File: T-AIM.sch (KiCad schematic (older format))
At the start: 21 parts, among them IC1 ATMEGA328PB-A

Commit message: Components wired
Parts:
- added C?: 1u, symbol CP1
- added C?: 10n, symbol CP1
- added C? (x2): 0.1u, symbol C
- added R?: 4.7k, symbol R
- added R?: 1k, symbol R
- added R?: 150, symbol R
- J?: value JY-MCU HC-05 Bluetooth Pins -> JY-MCU HC-05 Pins
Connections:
- net CS is gone; now on net 5V: J?.3 (P3)
- net VOUT is gone; now on net 5V: J?.2 (P2)
- net +9V: now also R?.1, R?.1, R?.1; no longer IC?.3 (VDD)
- net 5V: now also C?.1; no longer C?.1, C?.2, IC1.4 (VCC), R?.2, U?.VO
- net GND: now also IC?.1 (CTG), IC?.9 (EP), R?.2, C?.2, C?.2, C?.2; no longer C?.1
- net at IC1.18 (AVCC): now also C?.1, IC1.4 (VCC), U?.VO
- net at IC?.2 (CELL): now also C?.1, R?.2
- net BatteryLowAlert: now reaches IC?.5 (ALRT)
- net BatteryLowAlert: now also R?.2
- net FuelGaugeRestart: now reaches IC?.6 (QSTRT)
- net EN: now reaches J?.1 (P1)
- net State: now reaches J?.6 (P6)
- new net: C?.1, IC?.3 (VDD), R?.2
- no-connect marks 19 -> 18
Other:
- note added: "Alarm buzzer"
- note added: "Battery fuel gauge"
- note added: "Bluetooth Module"
- note added: "Interface Buttons"
- note added: "Sensors"
- note added: "Status LEDs"
- note added: "Voltage regulator"
- moved on the sheet: BZ?, C?, D?, IC1, IC?, J?, R?, SW?, U?

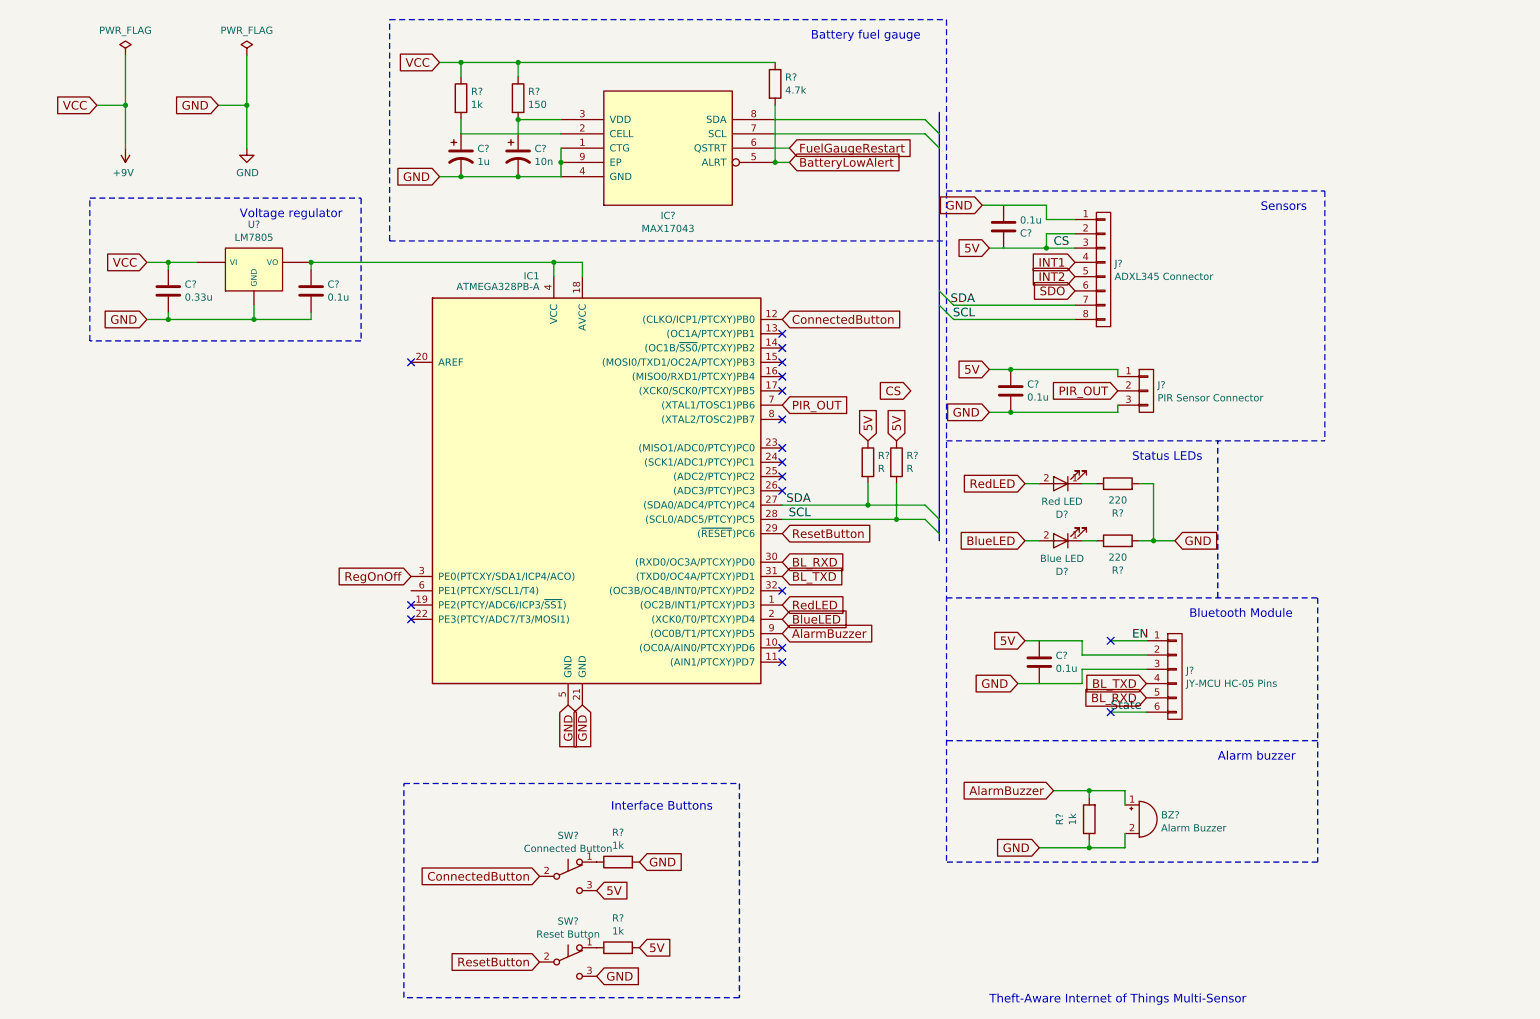
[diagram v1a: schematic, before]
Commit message: Schematics tidied up, added Vcc caps in front of MCU
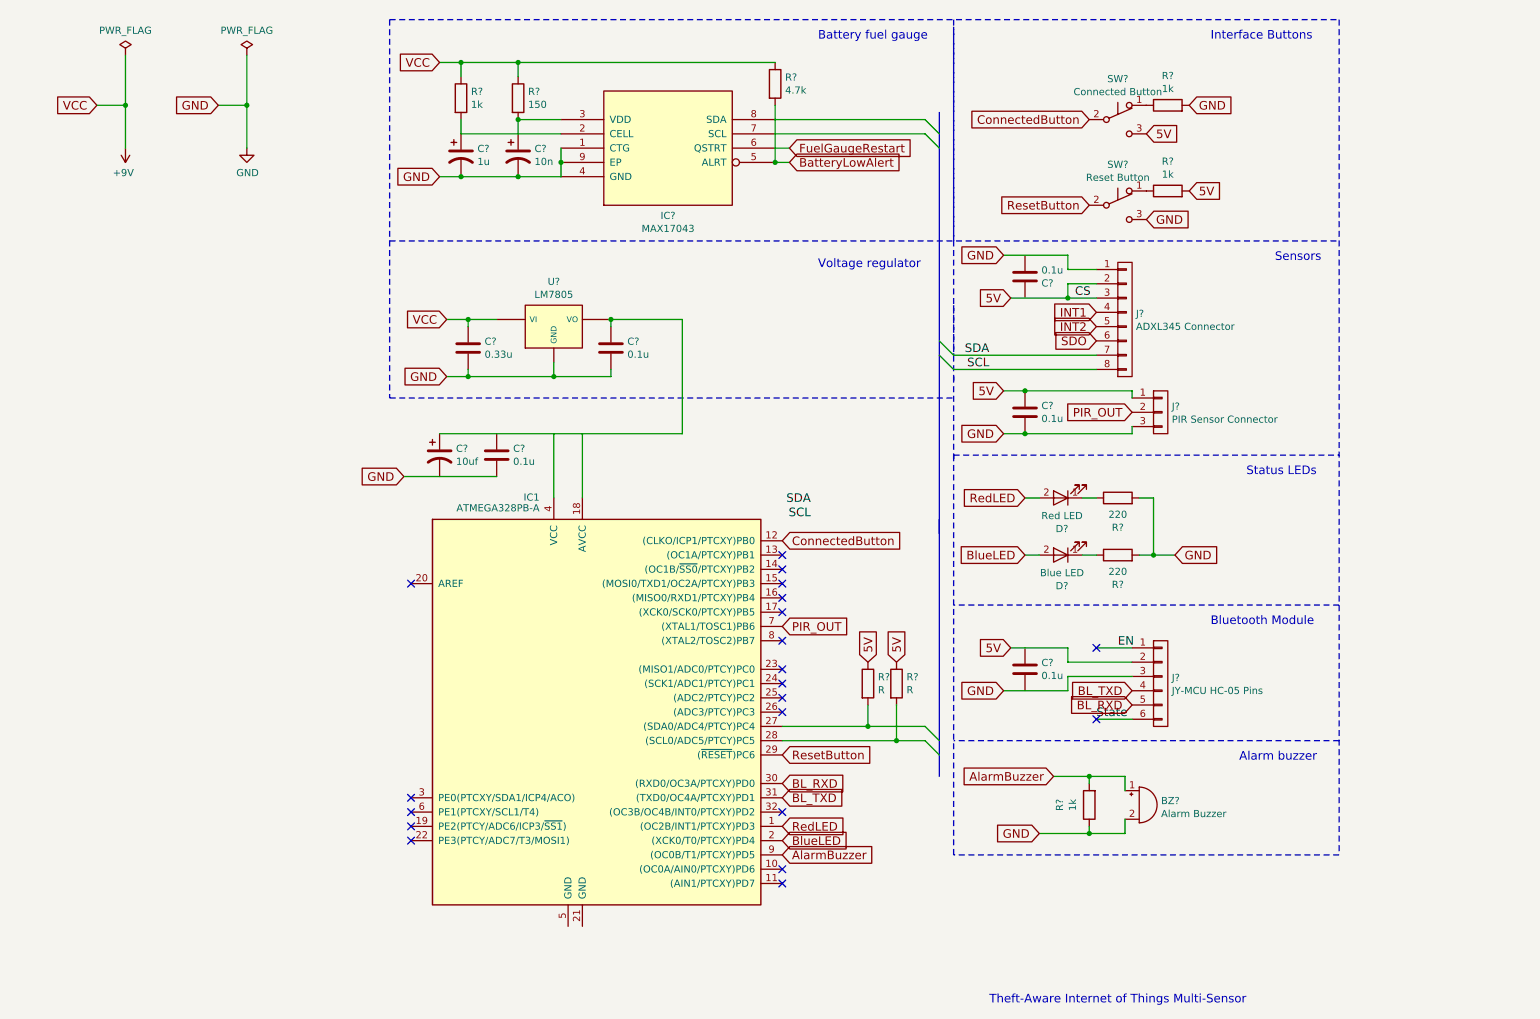
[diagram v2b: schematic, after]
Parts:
- added C?: 0.1u, symbol C
- added C?: 10uf, symbol CP1
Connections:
- net GND: now also C?.2; no longer IC1.21 (GND), IC1.5 (GND)
- net SCL: no longer IC1.28 ((SCL0/ADC5/PTCY)PC5), R?.2
- net SDA: no longer IC1.27 ((SDA0/ADC4/PTCY)PC4), R?.2
- net at C?.1, U?.VO: now also C?.1; no longer IC1.18 (AVCC), IC1.4 (VCC)
- net RegOnOff: no longer names the net of IC1.3 (PE0(PTCXY/SDA1/ICP4/ACO))
- new net: IC1.27 ((SDA0/ADC4/PTCY)PC4), R?.2
- new net: IC1.28 ((SCL0/ADC5/PTCY)PC5), R?.2
- no-connect marks 18 -> 20
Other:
- moved on the sheet: BZ?, C?, D?, IC1, J?, R?, SW?, U?

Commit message: Block name added
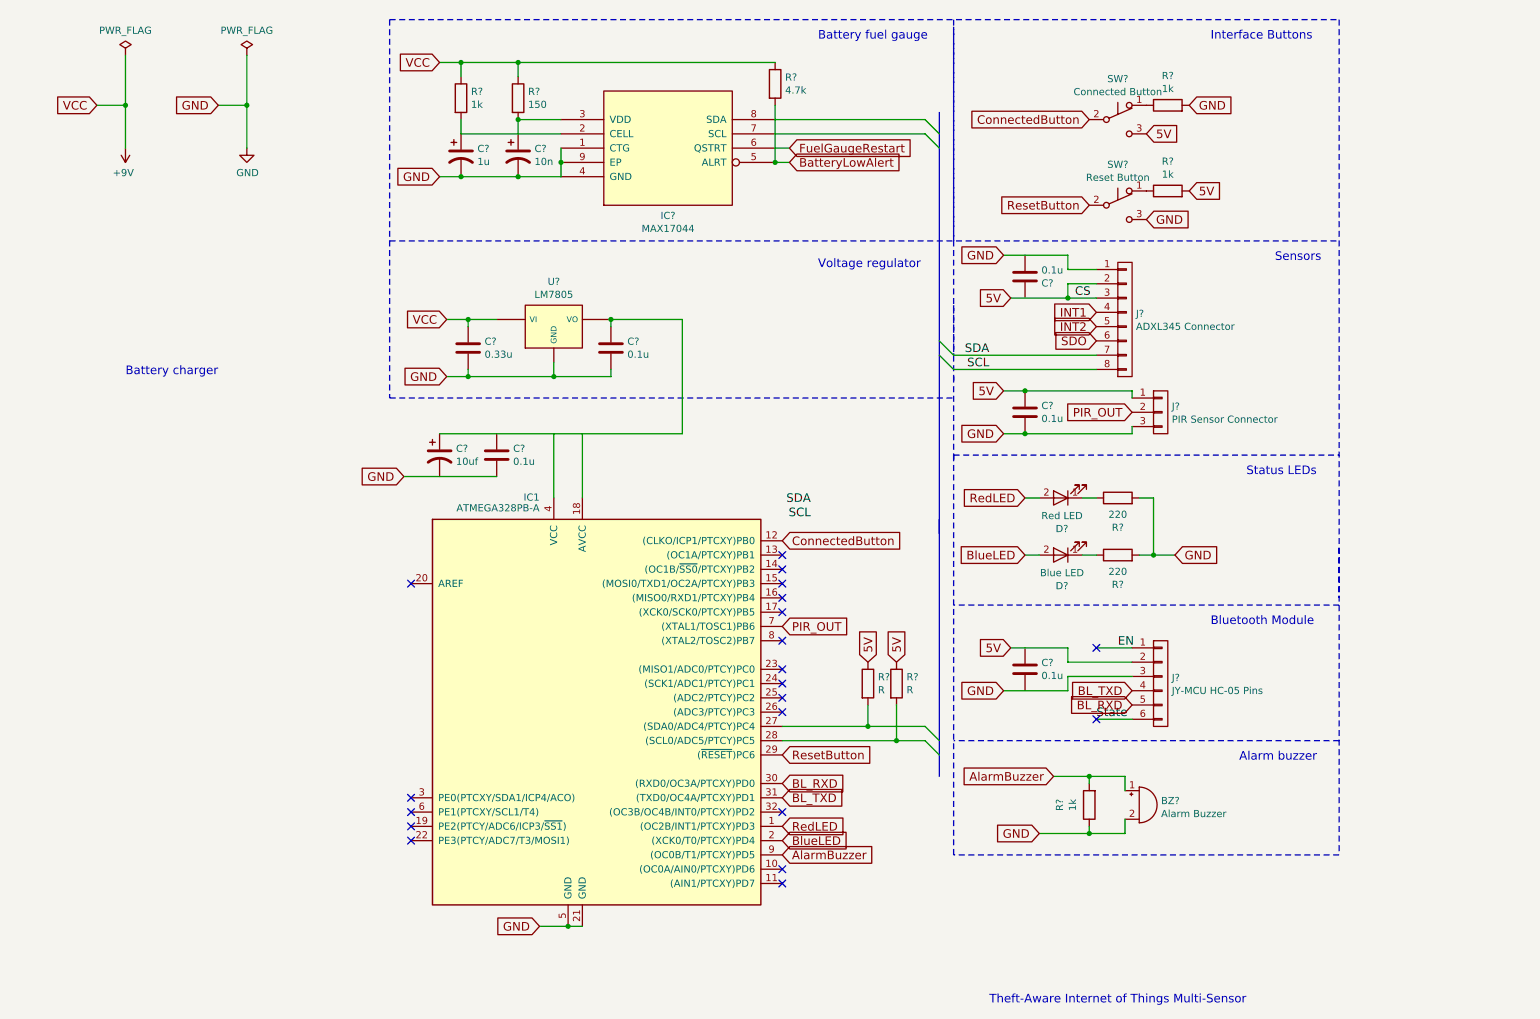
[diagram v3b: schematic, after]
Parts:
- IC?: value MAX17043 -> MAX17044
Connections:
- net GND: now also IC1.21 (GND), IC1.5 (GND)
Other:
- note added: "Battery charger"
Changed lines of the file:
@@
 LIBS:ttl_ieee
 LIBS:maxium
+LIBS:SparkFun
 LIBS:T-AIM-cache
 EELAYER 26 0
@@
 F 1 "Alarm Buzzer" H 8603 6038 50  0000 L CNN
 F 2 "" V 5825 1500 50  0001 C CNN
-F 3 "" V 5825 1500 50  0001 C CNN
+F 3 "http://www.puiaudio.com/pdf/AT-1220-TT-9-R.pdf" V 5825 1500 50  0001 C CNN
 	1    8450 6100
 	1    0    0    -1
@@
 P 5150 1500
 F 0 "IC?" H 5150 1027 50  0000 C CNN
-F 1 "MAX17043" H 5150 936 50  0000 C CNN
+F 1 "MAX17044" H 5150 936 50  0000 C CNN
 F 2 "" H -2600 -250 60  0001 C CNN
 F 3 "https://datasheets.maximintegrated.com/en/ds/MAX17043-MAX17044.pdf" H -2600 -250 60  0001 C CNN
@@
 Wire Notes Line
 	7150 2600 7150 2950
+Text GLabel 4250 6950 0    60   Input ~ 0
+GND
+Wire Wire Line
+	4550 6950 4250 6950
+Wire Notes Line
+	9850 4300 9850 4650
+Connection ~ 4450 6950
+Text Notes 1350 3100 0    60   ~ 0
+Battery charger
 $EndSCHEMATC

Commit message: Battery charger chip added to schematics
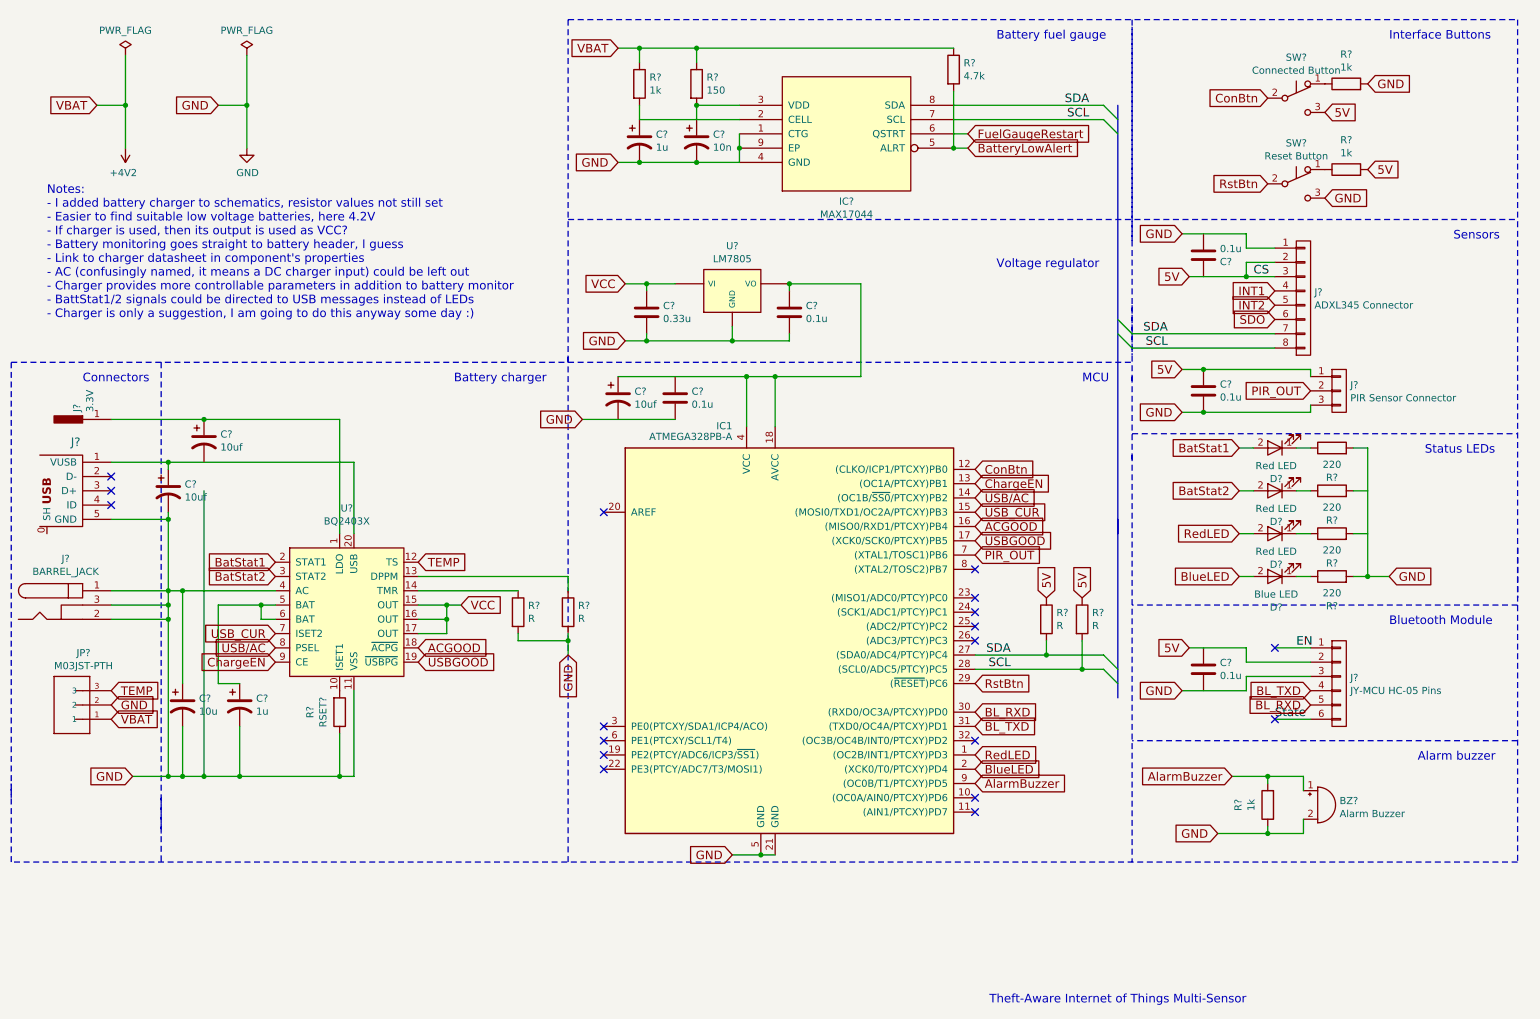
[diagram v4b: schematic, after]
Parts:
- added C? (x2): 10uf, symbol CP1
- added C?: 10u, symbol CP1
- added C?: 1u, symbol CP1
- added D? (x2): Red LED, symbol LED
- added J?: BARREL_JACK, symbol BARREL_JACK
- added J?: USBmicro, symbol USBmicro
- added J?: 3.3V, symbol CONN_01X01_MALE
- added JP?: M03JST-PTH, SparkFun-JST-3-PTH, symbol M03JST-PTH
- added R? (x2): 220, symbol R
- added R?: RSET?, symbol R
- added R? (x2): R, symbol R
- added U?: BQ2403X, symbol BQ2403X
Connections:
- net GND: now also C?.1, C?.2, C?.2, C?.2, J?.1, J?.2, J?.3, J?.5 (GND), JP?.2, R?.1, R?.2, R?.2, R?.2, U?.11 (VSS), U?.4 (AC); no longer R?.2
- net SCL: now also IC1.28 ((SCL0/ADC5/PTCY)PC5), IC?.7 (SCL), R?.2
- net SDA: now also IC1.27 ((SDA0/ADC4/PTCY)PC4), IC?.8 (SDA), R?.2
- net ChargeEN: now reaches IC1.13 ((OC1A/PTCXY)PB1)
- net ChargeEN: now also U?.9 (CE)
- net USB/AC: now reaches IC1.14 ((OC1B/~SS0~/PTCXY)PB2)
- net USB/AC: now also U?.8 (PSEL)
- net USB_CUR: now reaches IC1.15 ((MOSI0/TXD1/OC2A/PTCXY)PB3)
- net USB_CUR: now also U?.7 (ISET2)
- net ACGOOD: now reaches IC1.16 ((MISO0/RXD1/PTCXY)PB4)
- net ACGOOD: now also U?.18 (~ACPG)
- net USBGOOD: now reaches IC1.17 ((XCK0/SCK0/PTCXY)PB5)
- net USBGOOD: now also U?.19 (~USBPG)
- net at IC1.18 (AVCC): now also C?.1, C?.1, IC1.4 (VCC), U?.VO
- net +9V renamed +4V2
- net +4V2: now also JP?.1; no longer C?.1, U?.VI
- net ConnectedButton renamed ConBtn
- net ResetButton renamed RstBtn
- new net: C?.1, J?.1, U?.1 (LDO)
- new net: R?.2, U?.10 (ISET1)
- new net: R?.1, U?.13 (DPPM)
- new net: R?.1, U?.14 (TMR)
- new net: C?.1, J?.1 (VUSB), U?.20 (USB)
- new net: C?.1, U?.5 (BAT), U?.6 (BAT)
- new net: D?.1 (K), R?.1 (x2)
- new net BatStat1: D?.2 (A), U?.2 (STAT1)
- new net BatStat2: D?.2 (A), U?.3 (STAT2)
- new net TEMP: JP?.3, U?.12 (TS)
- new net VCC: C?.1, U?.15 (OUT), U?.16 (OUT), U?.17 (OUT), U?.VI
- no-connect marks 20 -> 18
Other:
- note added: "Connectors"
- note added: "MCU"
- note added: "Notes:\n- I added battery charger to schematics, resistor values not still set\n- Easier to find suitable low voltage batteries, here 4.2V\n- If charger is used, then its output is used as VCC?\n- Battery monitoring goes straight to battery header, I guess\n- Link to charger datasheet in component's properties\n- AC (confusingly named, it means a DC charger input) could be left out\n- Charger pro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"
- moved on the sheet: BZ?, C?, D?, IC1, IC?, J?, R?, SW?, U?
